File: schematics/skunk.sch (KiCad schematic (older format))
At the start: 50 parts

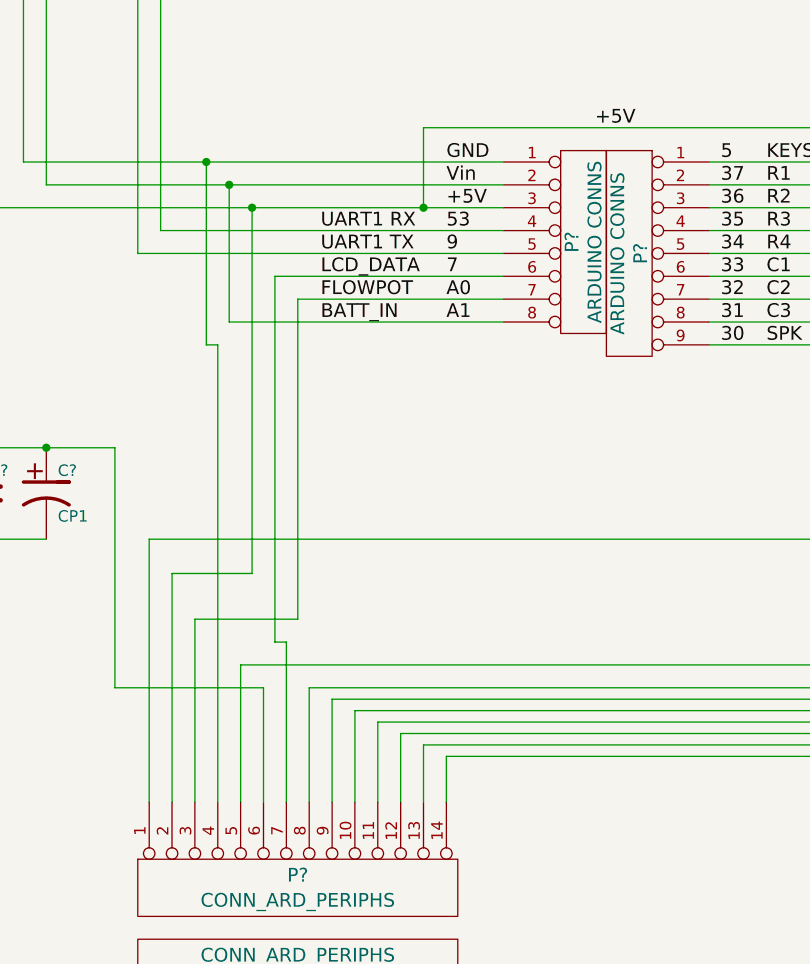
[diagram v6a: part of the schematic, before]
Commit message: Added battery sense input scaling
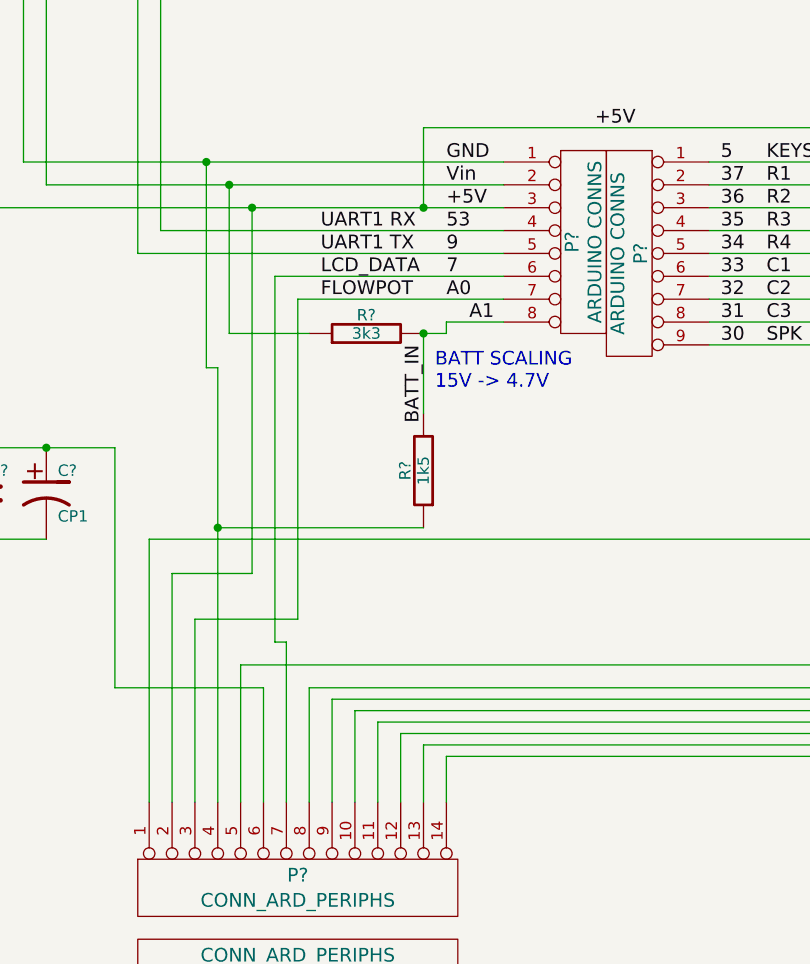
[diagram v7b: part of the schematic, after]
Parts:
- added R?: 3k3, symbol R
- added R?: 1k5, symbol R
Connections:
- net +12V: now also R?.1; no longer P?.8 (P8)
- net GND: now also R?.1
- new net A1: P?.8 (P8), R?.2, R?.2
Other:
- note added: "BATT SCALING\n15V -> 4.7V"
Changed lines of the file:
@@
-EESchema Schematic File Version 2  date Mon 15 Oct 2012 14:20:48 BST
+EESchema Schematic File Version 2  date Mon 15 Oct 2012 14:43:06 BST
 LIBS:power
 LIBS:device
@@
 Text Label 6100 4900 0    60   ~ 0
 A0
-Text Label 6100 5000 0    60   ~ 0
+Text Label 6200 5000 0    60   ~ 0
 A1
 Text Label 7300 4300 0    60   ~ 0
@@
 Text Label 5550 4900 0    60   ~ 0
 FLOWPOT
-Text Label 5550 5000 0    60   ~ 0
+Text Label 6000 5100 3    60   ~ 0
 BATT_IN
 Text Label 7500 4300 0    60   ~ 0
@@
 	5450 4900 5450 6300
 Wire Wire Line
-	6350 5000 5150 5000
-Wire Wire Line
-	5150 5000 5150 4400
+	5150 4400 5150 5050
 Connection ~ 5150 4400
 Wire Wire Line
@@
 	5400 6400 5350 6400
 Wire Wire Line
-	5100 7100 5100 5100
-Wire Wire Line
-	5100 5100 5050 5100
-Wire Wire Line
-	5050 5100 5050 4300
+	5050 4300 5050 5200
 Connection ~ 5050 4300
 Wire Wire Line
@@
 Text Notes 11400 8850 0    60   ~ 0
 CLAMP RESISTOR
+$Comp
+L R R?
+U 1 1 507C11BB
+P 5750 5050
+F 0 "R?" V 5830 5050 50  0000 C CNN
+F 1 "3k3" V 5750 5050 50  0000 C CNN
+	1    5750 5050
+	0    -1   -1   0
+$EndComp
+$Comp
+L R R?
+U 1 1 507C11CA
+P 6000 5650
+F 0 "R?" V 6080 5650 50  0000 C CNN
+F 1 "1k5" V 6000 5650 50  0000 C CNN
+	1    6000 5650
+	-1   0    0    1
+$EndComp
+Connection ~ 5100 5900
+Wire Wire Line
+	5100 5900 6000 5900
+Connection ~ 6000 5050
+Text Notes 6050 5300 0    60   ~ 0
+BATT SCALING\n15V -> 4.7V
+Wire Wire Line
+	6000 5400 6000 5050
+Wire Wire Line
+	6000 5050 6100 5050
+Wire Wire Line
+	6100 5050 6100 5000
+Wire Wire Line
+	6100 5000 6350 5000
+Wire Wire Line
+	5150 5050 5500 5050
+Wire Wire Line
+	5050 5200 5100 5200
+Wire Wire Line
+	5100 5200 5100 7100
 $EndSCHEMATC

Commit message: Added connector gender labels
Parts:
- added K?: CONN_ARD_RS232_M, symbol CONN_3
- J?: value DB9_ARD_BOX -> DB9_ARD_BOX_F
- J?: value DB9_ARD_BOX -> DB9_ARD_BOX_M
- J?: value DB9_FLOWMETER -> DB9_FLOWMETER_F
- J? (x2): value DB25_PERIPHS -> DB25_PERIPHS_F
- J? (x2): value DB25_PERIPHS -> DB25_PERIPHS_M
- K?: value CONN_ARD_RS232 -> CONN_ARD_RS232_F
- P?: value CONN_BAT_1 -> CONN_BAT_F
- P?: value CONN_BAT_1 -> CONN_BAT_M
- P?: value CONN_ARD_POWER -> CONN_ARD_POWER_F
- P?: value CONN_ARD_PERIPHS -> CONN_ARD_PERIPHS_F
- P?: value CONN_2 -> CONN_ARD_POWER_M
- P?: value CONN_ARD_PERIPHS -> CONN_ARD_PERIPHS_M
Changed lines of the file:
@@
-EESchema Schematic File Version 2  date Mon 15 Oct 2012 14:43:06 BST
+EESchema Schematic File Version 2  date Mon 15 Oct 2012 22:10:27 BST
 LIBS:power
 LIBS:device
@@
 P 9200 9450
 F 0 "J?" H 9250 10800 70  0000 C CNN
-F 1 "DB25_PERIPHS" H 8950 8100 70  0000 C CNN
+F 1 "DB25_PERIPHS_F" H 8750 8100 70  0000 C CNN
 	1    9200 9450
 	-1   0    0    -1
@@
 P 7200 9450
 F 0 "J?" H 7250 10800 70  0000 C CNN
-F 1 "DB25_PERIPHS" H 7000 8100 70  0000 C CNN
+F 1 "DB25_PERIPHS_F" H 6800 8100 70  0000 C CNN
 	1    7200 9450
 	1    0    0    -1
@@
 P 5450 7850
 F 0 "P?" V 5420 7850 60  0000 C CNN
-F 1 "CONN_ARD_PERIPHS" V 5530 7850 60  0000 C CNN
+F 1 "CONN_ARD_PERIPHS_F" V 5530 7850 60  0000 C CNN
 	1    5450 7850
 	0    -1   -1   0
@@
 P 7600 1800
 F 0 "K?" V 7550 1800 50  0000 C CNN
-F 1 "CONN_ARD_RS232" H 7400 1500 40  0000 C CNN
+F 1 "CONN_ARD_RS232_F" H 7400 2000 40  0000 C CNN
 	1    7600 1800
 	-1   0    0    -1
@@
 P 15500 1150
 F 0 "J?" H 15500 1700 70  0000 C CNN
-F 1 "DB9_FLOWMETER" H 15500 600 70  0000 C CNN
+F 1 "DB9_FLOWMETER_F" H 15400 600 70  0000 C CNN
 	1    15500 1150
 	1    0    0    -1
@@
 P 8900 1800
 F 0 "J?" H 8900 2350 70  0000 C CNN
-F 1 "DB9_ARD_BOX" H 8650 1200 70  0000 C CNN
+F 1 "DB9_ARD_BOX_M" H 8600 1200 70  0000 C CNN
 	1    8900 1800
 	1    0    0    -1
@@
 P 9250 1800
 F 0 "J?" H 9250 2350 70  0000 C CNN
-F 1 "DB9_ARD_BOX" H 9000 1200 70  0000 C CNN
+F 1 "DB9_ARD_BOX_F" H 8950 1200 70  0000 C CNN
 	1    9250 1800
 	-1   0    0    -1
@@
 P 2750 3300
 F 0 "P?" V 2700 3300 40  0000 C CNN
-F 1 "CONN_ARD_POWER" H 2550 3500 40  0000 C CNN
+F 1 "CONN_ARD_POWER_F" H 2550 3500 40  0000 C CNN
 	1    2750 3300
 	1    0    0    1
@@
 P 900 1900
 F 0 "P?" V 850 1900 40  0000 C CNN
-F 1 "CONN_BAT_1" V 1050 1900 40  0000 C CNN
+F 1 "CONN_BAT_M" V 1050 1900 40  0000 C CNN
 	1    900  1900
 	0    -1   -1   0
@@
 P 900 1500
 F 0 "P?" V 850 1500 40  0000 C CNN
-F 1 "CONN_BAT_1" V 1050 1500 40  0000 C CNN
+F 1 "CONN_BAT_F" V 1050 1500 40  0000 C CNN
 	1    900  1500
 	0    -1   1    0
@@
 P 8750 9450
 F 0 "J?" H 8800 10800 70  0000 C CNN
-F 1 "DB25_PERIPHS" H 8650 8100 70  0000 C CNN
+F 1 "DB25_PERIPHS_M" H 8700 8100 70  0000 C CNN
 	1    8750 9450
 	1    0    0    -1
@@
 P 7650 9450
 F 0 "J?" H 7700 10800 70  0000 C CNN
-F 1 "DB25_PERIPHS" H 7450 8100 70  0000 C CNN
+F 1 "DB25_PERIPHS_M" H 7550 8100 70  0000 C CNN
 	1    7650 9450
 	-1   0    0    -1
@@
 	6400 2350 6400 1800
 Wire Wire Line
-	6400 1800 7200 1800
-Wire Wire Line
 	4750 4700 4750 2250
 Wire Wire Line
@@
 Wire Wire Line
 	6300 2250 6300 1700
-Wire Wire Line
-	6300 1700 7200 1700
 Wire Wire Line
 	4750 4700 6350 4700
@@
 P 3050 3300
 F 0 "P?" V 3000 3300 40  0000 C CNN
-F 1 "CONN_2" V 3100 3300 40  0000 C CNN
+F 1 "CONN_ARD_POWER_M" H 2850 3500 40  0000 C CNN
 	1    3050 3300
 	-1   0    0    1
@@
 P 5450 7450
 F 0 "P?" V 5420 7450 60  0000 C CNN
-F 1 "CONN_ARD_PERIPHS" V 5530 7450 60  0000 C CNN
+F 1 "CONN_ARD_PERIPHS_M" V 5530 7450 60  0000 C CNN
 	1    5450 7450
 	0    -1   1    0
@@
 Wire Wire Line
 	5100 5200 5100 7100
+$Comp
+L CONN_3 K?
+U 1 1 507C8214
+P 7350 1800
+F 0 "K?" V 7300 1800 50  0000 C CNN
+F 1 "CONN_ARD_RS232_M" H 7150 2000 40  0000 C CNN
+	1    7350 1800
+	1    0    0    -1
+$EndComp
+Wire Wire Line
+	6400 1800 6600 1800
+Wire Wire Line
+	6300 1700 6450 1700
 $EndSCHEMATC
